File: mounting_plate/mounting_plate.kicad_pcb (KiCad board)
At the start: 2 copper layers, 167.6 x 81.3 mm, 9 parts

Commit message: update mounting plate pdf
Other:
- board text added: "PELICAN GO CASE G40"
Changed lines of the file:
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@@
   (general
     (thickness 1.6)
-    (drawings 43)
+    (drawings 44)
     (tracks 0)
     (zones 0)
@@
       (excludeedgelayer true)
       (linewidth 0.100000)
-      (plotframeref false)
+      (plotframeref true)
       (viasonmask false)
       (mode 1)
@@
       (padsonsilk false)
       (subtractmaskfromsilk false)
-      (outputformat 1)
+      (outputformat 4)
       (mirror false)
       (drillshape 0)
       (scaleselection 1)
-      (outputdirectory "gerber_files/"))
+      (outputdirectory ""))
   )
   (net 0 "")
@@
       (effects (font (size 1 1) (thickness 0.15)))
     )
-    (fp_text user %R (at 0.3 0 90) (layer F.Fab) hide
-      (effects (font (size 1 1) (thickness 0.15)))
-    )
-    (fp_circle (center 0 0) (end 3.2 0) (layer Cmts.User) (width 0.15))
-    (fp_circle (center 0 0) (end 3.45 0) (layer F.CrtYd) (width 0.05))
+    (fp_circle (center 0 0) (end 3.2 0) (layer Cmts.User) (width 0.15))
+    (fp_circle (center 0 0) (end 3.45 0) (layer F.CrtYd) (width 0.05))
+    (fp_text user %R (at 0.3 0 90) (layer F.Fab) hide
+      (effects (font (size 1 1) (thickness 0.15)))
+    )
     (pad 1 np_thru_hole circle (at 0 0 90) (size 3.2 3.2) (drill 3.2) (layers *.Cu *.Mask))
   )
@@
       (effects (font (size 1 1) (thickness 0.15)))
     )
-    (fp_text user %R (at 0.3 0 90) (layer F.Fab) hide
-      (effects (font (size 1 1) (thickness 0.15)))
-    )
-    (fp_circle (center 0 0) (end 3.2 0) (layer Cmts.User) (width 0.15))
-    (fp_circle (center 0 0) (end 3.45 0) (layer F.CrtYd) (width 0.05))
+    (fp_circle (center 0 0) (end 3.2 0) (layer Cmts.User) (width 0.15))
+    (fp_circle (center 0 0) (end 3.45 0) (layer F.CrtYd) (width 0.05))
+    (fp_text user %R (at 0.3 0 90) (layer F.Fab) hide
+      (effects (font (size 1 1) (thickness 0.15)))
+    )
     (pad 1 np_thru_hole circle (at 0 0 270) (size 3.2 3.2) (drill 3.2) (layers *.Cu *.Mask))
   )
@@
       (effects (font (size 1 1) (thickness 0.15)))
     )
-    (fp_text user %R (at 0.3 0 90) (layer F.Fab) hide
-      (effects (font (size 1 1) (thickness 0.15)))
-    )
-    (fp_circle (center 0 0) (end 3.2 0) (layer Cmts.User) (width 0.15))
-    (fp_circle (center 0 0) (end 3.45 0) (layer F.CrtYd) (width 0.05))
+    (fp_circle (center 0 0) (end 3.2 0) (layer Cmts.User) (width 0.15))
+    (fp_circle (center 0 0) (end 3.45 0) (layer F.CrtYd) (width 0.05))
+    (fp_text user %R (at 0.3 0 90) (layer F.Fab) hide
+      (effects (font (size 1 1) (thickness 0.15)))
+    )
     (pad 1 np_thru_hole circle (at 0 0 90) (size 3.2 3.2) (drill 3.2) (layers *.Cu *.Mask))
   )
@@
   (module Adafruit:SCD-30_CO2_Sensor (layer F.Cu)
     (at 170.18 104.14)
-    (fp_text reference REF** (at 0 -16.51) (layer F.SilkS)
-      (effects (font (size 1 1) (thickness 0.15)))
-    )
-    (fp_text value SCD-30_CO2_Sensor (at 0 -14.605) (layer F.Fab)
-      (effects (font (size 1 1) (thickness 0.15)))
-    )
-    (fp_text user SENSIRION (at 16.51 -5.08 90) (layer F.SilkS)
-      (effects (font (size 1 1) (thickness 0.15)))
-    )
-    (fp_text user SCD-30 (at -19.05 0 270 unlocked) (layer F.SilkS)
+    (fp_text reference REF** (at 0 -3.81) (layer F.Fab)
+      (effects (font (size 1 1) (thickness 0.15)))
+    )
+    (fp_text value SCD-30_CO2_Sensor (at 0 -1.905) (layer F.SilkS)
       (effects (font (size 1 1) (thickness 0.15)))
     )
@@
     (fp_line (start 0 -12.7) (end 0 12.7) (layer F.SilkS) (width 0.12))
     (fp_line (start -25.4 0) (end 25.4 0) (layer F.SilkS) (width 0.12))
+    (fp_text user SENSIRION (at 16.51 -5.08 90) (layer F.SilkS)
+      (effects (font (size 1 1) (thickness 0.15)))
+    )
+    (fp_text user SCD-30 (at -19.05 0 270 unlocked) (layer F.SilkS)
+      (effects (font (size 1 1) (thickness 0.15)))
+    )
     (pad "" np_thru_hole circle (at -22.86 -10.16 90) (size 3 3) (drill 2.6) (layers *.Cu *.Mask))
     (pad "" np_thru_hole circle (at -22.86 10.16 180) (size 3 3) (drill 2.6) (layers *.Cu *.Mask))
@@
   (module Adafruit:PMSA003I_Air_Quality_Sensor (layer F.Cu)
     (at 170.18 66.675)
-    (fp_text reference REF** (at 0 -22.225) (layer F.SilkS)
-      (effects (font (size 1 1) (thickness 0.15)))
-    )
-    (fp_text value PMSA003I_Air_Quality_Sensor (at 0 -20.32) (layer F.Fab)
-      (effects (font (size 1 1) (thickness 0.15)))
-    )
-    (fp_text user PLANTOWER (at 6.35 7.62) (layer F.SilkS)
+    (fp_text reference REF** (at 0.635 -0.635) (layer F.Fab)
+      (effects (font (size 1 1) (thickness 0.15)))
+    )
+    (fp_text value PMSA003I_Air_Quality_Sensor (at 0 1.905) (layer F.SilkS)
       (effects (font (size 1 1) (thickness 0.15)))
     )
@@
     (fp_line (start 15.875 -16.51) (end 16.51 -17.145) (layer F.SilkS) (width 0.12))
     (fp_line (start 15.875 -16.51) (end 15.24 -17.145) (layer F.SilkS) (width 0.12))
+    (fp_text user PLANTOWER (at 6.35 7.62) (layer F.SilkS)
+      (effects (font (size 1 1) (thickness 0.15)))
+    )
     (pad "" np_thru_hole circle (at -22.86 15.24) (size 3 3) (drill 2.6) (layers *.Cu *.Mask))
     (pad "" np_thru_hole circle (at -22.86 -15.24) (size 3 3) (drill 2.6) (layers *.Cu *.Mask))
@@
   (module Adafruit:PyBadge_mechanical (layer F.Cu)
     (at 82.55 78.74 270)
-    (fp_text reference REF** (at 0 -31.115 90) (layer F.SilkS)
-      (effects (font (size 1 1) (thickness 0.15)))
-    )
-    (fp_text value PyBadge_mechanical (at 0 -29.845 90) (layer F.Fab)
+    (fp_text reference REF** (at -3.81 0 180) (layer F.Fab)
+      (effects (font (size 1 1) (thickness 0.15)))
+    )
+    (fp_text value PyBadge_mechanical (at -1.905 0 180) (layer F.SilkS)
       (effects (font (size 1 1) (thickness 0.15)))
     )
@@
     (pad "" np_thru_hole circle (at 38.735 -22.86 270) (size 3 3) (drill 2.6) (layers *.Cu *.Mask))
   )
+  (gr_text "PELICAN GO CASE G40" (at 127.635 114.935) (layer F.SilkS)
+    (effects (font (size 1.5 1.5) (thickness 0.3)))
+  )
   (gr_text M3 (at 199.39 107.315) (layer F.SilkS)

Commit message: update g40 mounting plate drawing
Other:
- board text added: "BOTTOM"

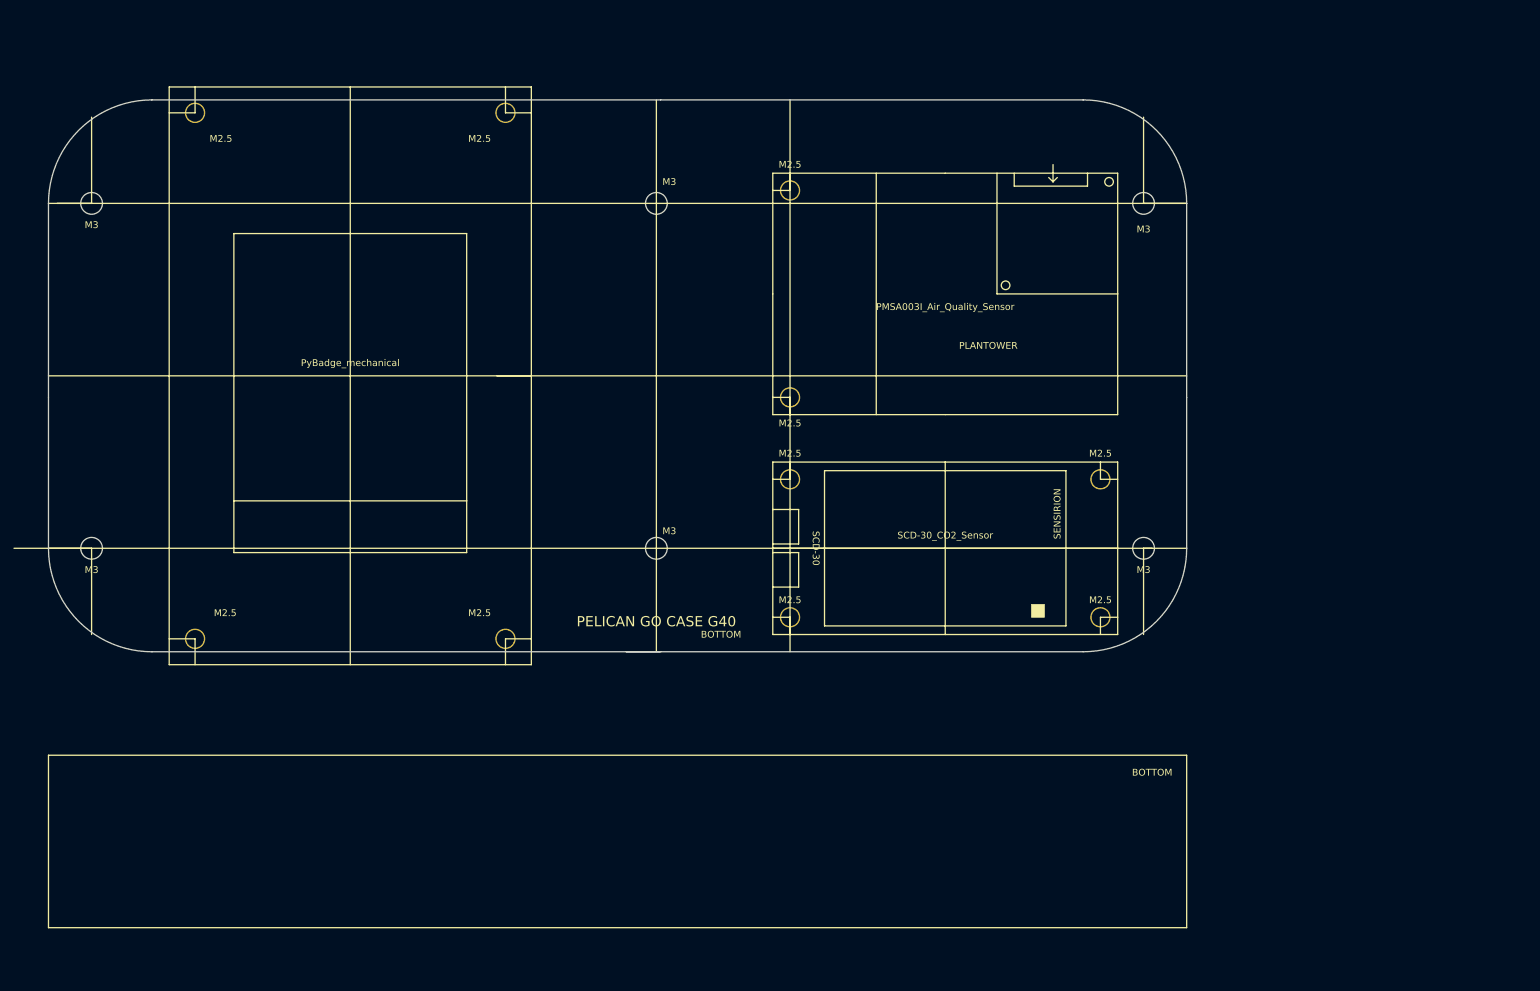
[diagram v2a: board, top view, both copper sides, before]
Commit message: update mounting plate drawing
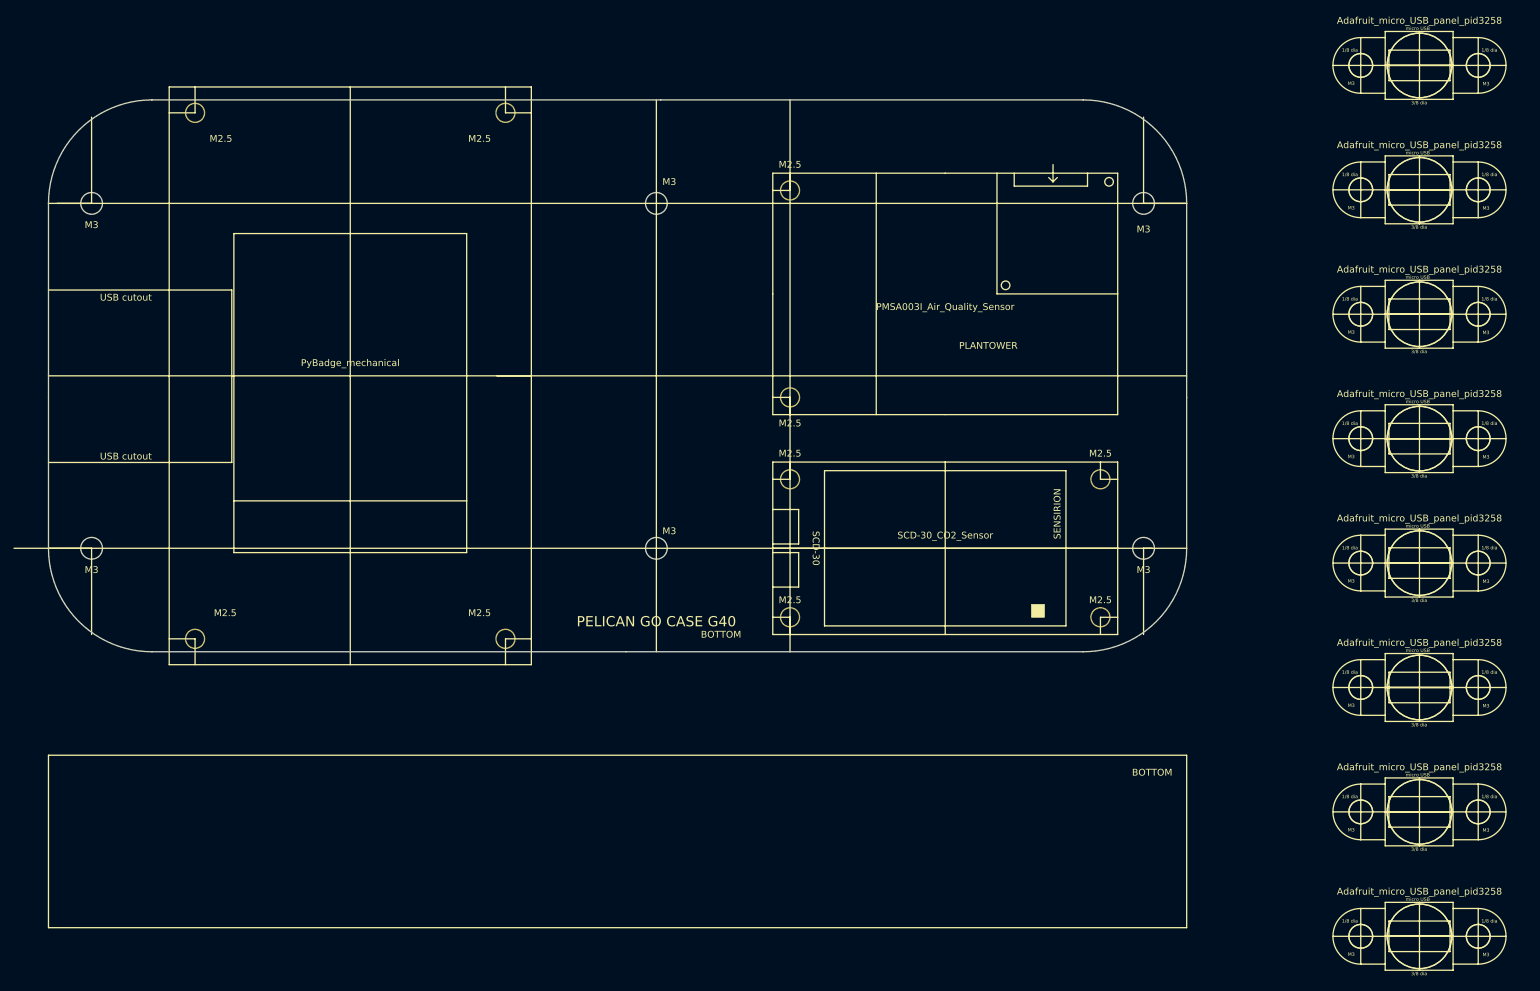
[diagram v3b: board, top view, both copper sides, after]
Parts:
- added REF**: Adafruit_micro_USB_panel_pid3258, Adafruit:Adafruit_micro_USB_panel_pid3258, F.Cu at (240.0, 143.0)
- added REF**: Adafruit_micro_USB_panel_pid3258, Adafruit:Adafruit_micro_USB_panel_pid3258, F.Cu at (240.0, 161.3)
- added REF**: Adafruit_micro_USB_panel_pid3258, Adafruit:Adafruit_micro_USB_panel_pid3258, F.Cu at (240.0, 124.6)
- added REF**: Adafruit_micro_USB_panel_pid3258, Adafruit:Adafruit_micro_USB_panel_pid3258, F.Cu at (240.0, 88.0)
- added REF**: Adafruit_micro_USB_panel_pid3258, Adafruit:Adafruit_micro_USB_panel_pid3258, F.Cu at (240.0, 106.3)
- added REF**: Adafruit_micro_USB_panel_pid3258, Adafruit:Adafruit_micro_USB_panel_pid3258, F.Cu at (240.0, 69.7)
- added REF**: Adafruit_micro_USB_panel_pid3258, Adafruit:Adafruit_micro_USB_panel_pid3258, F.Cu at (240.0, 51.3)
- added REF**: Adafruit_micro_USB_panel_pid3258, Adafruit:Adafruit_micro_USB_panel_pid3258, F.Cu at (240.0, 33.0)
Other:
- outline, holes or cut-outs redrawn
- board text added: "USB cutout"
